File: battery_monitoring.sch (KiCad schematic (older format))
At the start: 17 parts, among them P1 TC_SWD, SW4 SW_SP3T, U7 STM32F030F4Px

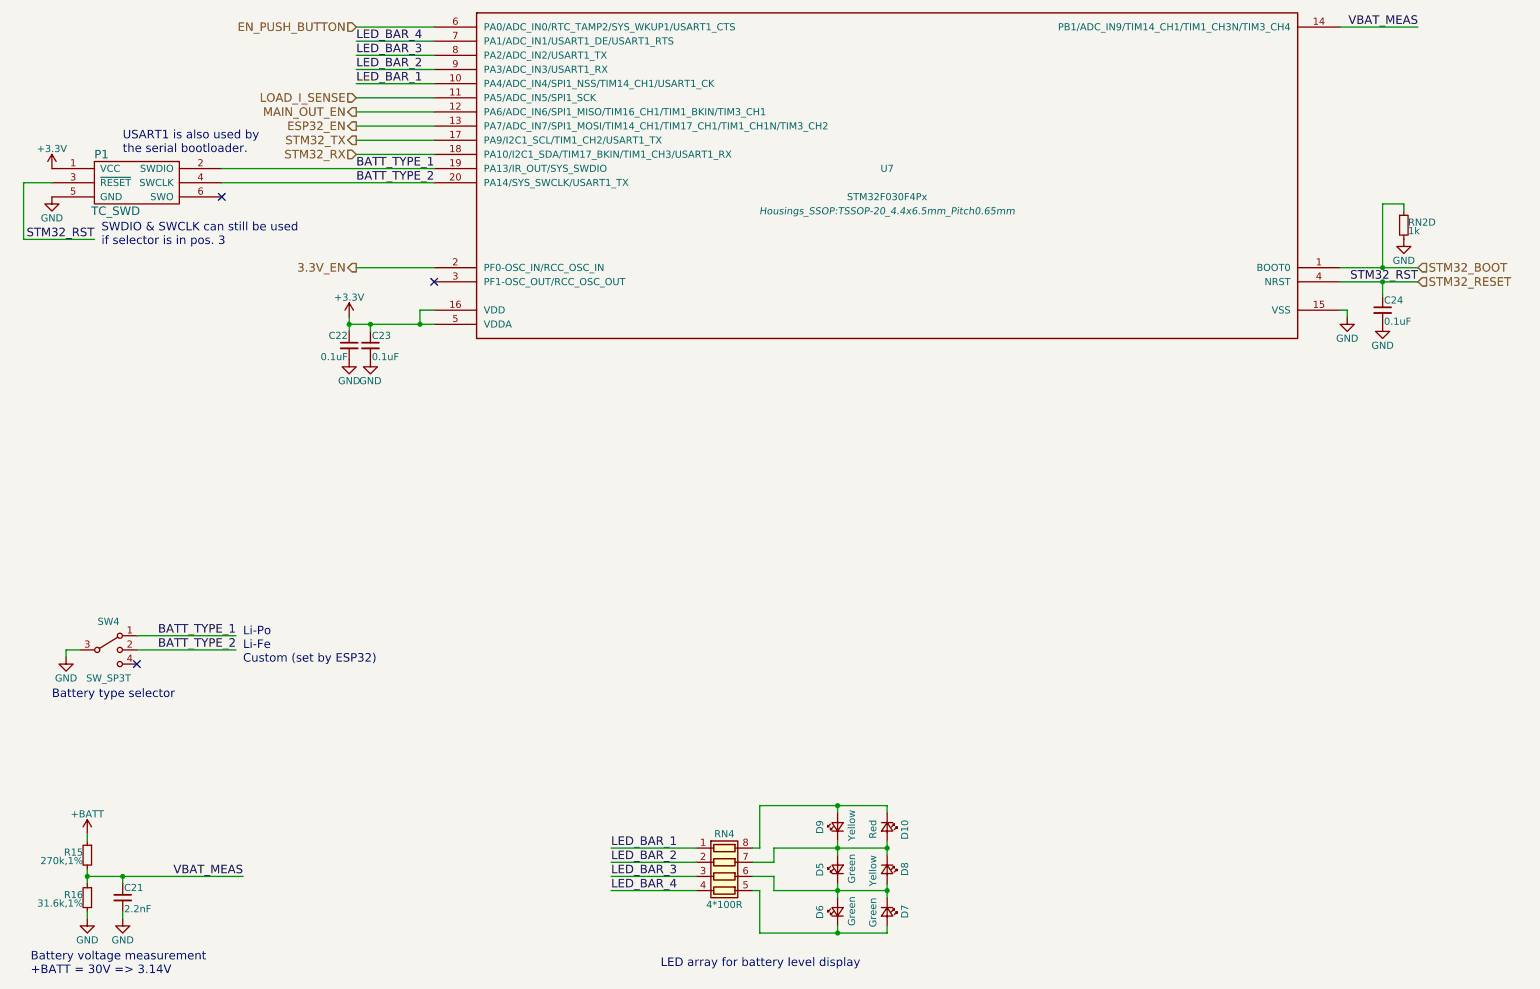
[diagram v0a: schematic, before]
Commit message: v2.0 - audio circuitry on a separate board ; optimized connectors and lots of improvements
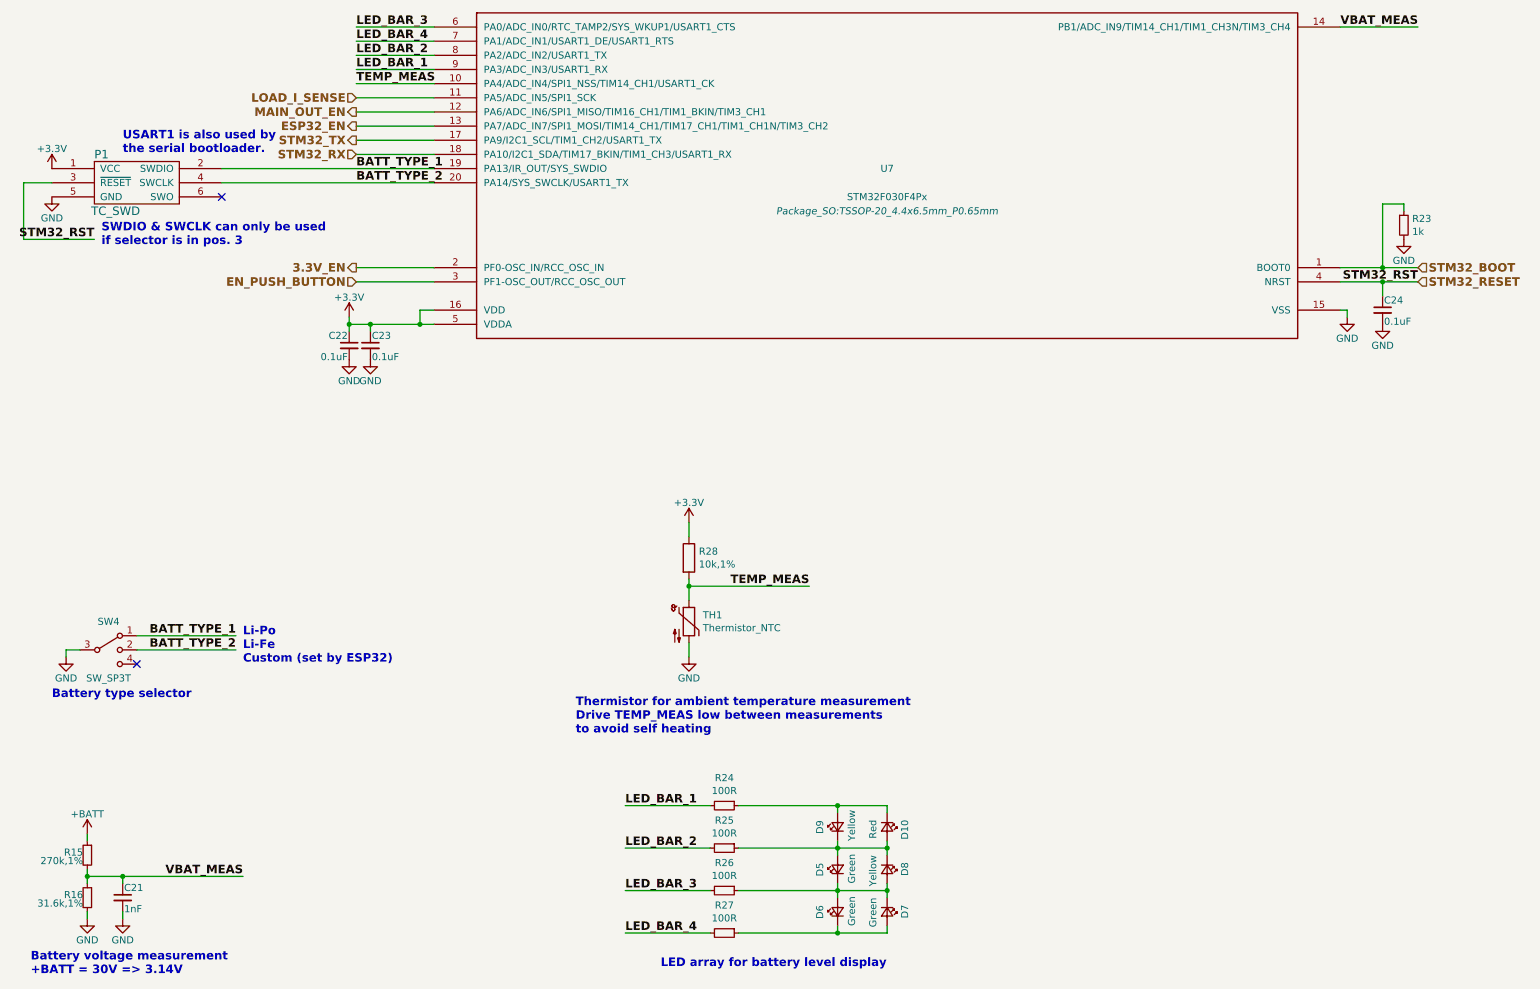
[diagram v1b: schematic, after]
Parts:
- removed RN2: 1k, Resistors_SMD:R_Array_Convex_4x0402, symbol KXKM_audio_battery_module-rescue:R_Pack04_Unit
- removed RN4: 4*100R, Resistors_SMD:R_Array_Convex_4x0402, symbol KXKM_audio_battery_module-rescue:R_Pack04
- added R23: 1k, Resistor_SMD:R_0603_1608Metric, symbol Device:R_Small
- added R24, R25, R26, R27: 100R, Resistor_SMD:R_0603_1608Metric, symbol Device:R_Small
- added R28: 10k,1%, Resistor_SMD:R_0603_1608Metric, symbol Device:R
- added TH1: Thermistor_NTC, Resistor_SMD:R_0603_1608Metric, symbol Device:Thermistor_NTC
- C21: value 2.2nF -> 1nF; footprint Capacitors_SMD:C_0603 -> Capacitor_SMD:C_0603_1608Metric
- C22, C23, C24: footprint Capacitors_SMD:C_0603 -> Capacitor_SMD:C_0603_1608Metric
- D10, D5, D6, D7, D8, D9: footprint LEDs:LED_0603 -> LED_SMD:LED_0603_1608Metric
- P1: footprint Connectors:Tag-Connect_TC2030-IDC-NL -> Connector:Tag-Connect_TC2030-IDC-NL_2x03_P1.27mm_Vertical
- R15, R16: footprint Resistors_SMD:R_0603 -> Resistor_SMD:R_0603_1608Metric
- SW4: footprint Buttons_Switches_SMD:SW_SP3T_PCM13 -> Button_Switch_SMD:SW_SP3T_PCM13
- U7: footprint Housings_SSOP:TSSOP-20_4.4x6.5mm_Pitch0.65mm -> Package_SO:TSSOP-20_4.4x6.5mm_P0.65mm
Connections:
- net +3V3: now also R28.1
- net EN_PUSH_BUTTON: now also U7.3 (PF1-OSC_OUT/RCC_OSC_OUT); no longer U7.6 (PA0/ADC_IN0/RTC_TAMP2/SYS_WKUP1/USART1_CTS)
- net GND: now also R23.2, TH1.2
- net LED_BAR_1: now also U7.9 (PA3/ADC_IN3/USART1_RX), R24.2; no longer U7.10 (PA4/ADC_IN4/SPI1_NSS/TIM14_CH1/USART1_CK)
- net LED_BAR_2: now also U7.8 (PA2/ADC_IN2/USART1_TX), R25.2; no longer U7.9 (PA3/ADC_IN3/USART1_RX)
- net LED_BAR_3: now also U7.6 (PA0/ADC_IN0/RTC_TAMP2/SYS_WKUP1/USART1_CTS), R26.2; no longer U7.8 (PA2/ADC_IN2/USART1_TX)
- net LED_BAR_4: now also R27.2
- net STM32_BOOT: now also R23.1
- net at D6.1 (K), D7.2 (A): now also R27.1
- net at D5.1 (K), D6.2 (A), D7.1 (K)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: now also R26.1
- net at D10.2 (A), D5.2 (A), D8.1 (K)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: now also R25.1
- net at D10.1 (K), D9.2 (A): now also R24.1
- new net TEMP_MEAS: R28.2, TH1.1, U7.10 (PA4/ADC_IN4/SPI1_NSS/TIM14_CH1/USART1_CK)
- no-connect marks 3 -> 2
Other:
- note added: "SWDIO & SWCLK can only be used\nif selector is in pos. 3"
- note added: "Thermistor for ambient temperature measurement\nDrive TEMP_MEAS low between measurements\nto avoid self heating"
- note removed: "SWDIO & SWCLK can still be used\nif selector is in pos. 3"
